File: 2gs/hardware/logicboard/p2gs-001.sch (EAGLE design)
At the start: 66 parts, among them J1 MKR, J10 1-Wire, J2 GPIO, J3 Vcc, J5 SPI, J6 LED, J7 DIN5, K1 G5V1, Q1 220mA/50V/3.5Ω, Q2 220mA/50V/3.5Ω, T1 2SC1815

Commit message: Routed.
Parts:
- removed A, B: (no value), wirepad:SMD2
- removed C1: 22u, rcl:C-EU025-050X050
- removed C10, C11, C4: 100n, rcl:C-EU025-024X044
- removed C12, C13, C3: 1u, rcl:C-EU050-024X044
- removed C2: 470n, rcl:C-EU050-024X044
- removed C5: 10n, resistor:C-EU025-024X044
- removed DISP1: AQM0802A-RN-GBW, AQM0802A-RN-GBW:AQM0802A-RN-GBW
- removed DISP2: MNTR, pinhead:PINHD-1X4
- removed F1: 1.8A, fuse:TE5
- removed H1, H2: STAND-OFF, SparkFun-Hardware:STAND-OFF
- removed J10: 1-Wire, SparkFun-Connectors:CONN_03JST-PTH-VERT
- removed J20: (no value), SparkFun-Connectors:CONN_041.27MM
- removed J3: Vcc, SparkFun-Connectors:CONN_02JST-PTH-2
- removed J5: SPI, SparkFun-Connectors:CONN_061.27MM
- removed J6: LED, SparkFun-Connectors:CONN_03JST-PTH-VERT
- removed JP1: PWRSEL, pinhead:PINHD-2X3
- removed JP2: RTC, SparkFun-Connectors:CONN_05
- removed JP4: RLYJMP, pinhead:PINHD-1X2
- removed JP5: PWR, pinhead:PINHD-1X3
- removed JP6: LED, pinhead:PINHD-1X3
- removed K1: G5V1, relay:G5V1
- removed R1, R3: 1k, resistor:R-EU_0204/5
- removed R101, R102, R103, R104: 10k, rcl:R-EU_M2012
- removed R2: 47k, resistor:R-EU_0204/5
- removed RN2: 4.7k, resistor-net:RN04
- removed RN4: 220, resistor-dil:8R-N
- removed RZ1***, RZ2***, RZ3**, RZ4**, VCCBRIDGE***: Inf, rcl:R-EU_M2012
- removed T1: 2SC1815, transistor:2SC1815
- removed V1: 5V, v-reg:78XXL
- removed VDDBRIDGE: 0, rcl:R-EU_M2012
- added D10, D11, D12, D13, D14, D15, D16, D4, D5, D6, D7, D8, D9: 200mA/100V/1V, SparkFun-DiscreteSemi:DIODE-1N4148
- added D20: DIODE-1N4148, SparkFun-DiscreteSemi:DIODE-1N4148
- added LD1: Red/Green, led:DUOLED-RG-C
- added Q10, Q11, Q12, Q13, Q14, Q15, Q16, Q3, Q4, Q5, Q6, Q7, Q8, Q9: 60V/32A/35mΩ, SparkFun-DiscreteSemi:MOSFET-NCH-FQP30N06L
- added R6: 220, resistor:R-EU_0204/5
- added X1: ADAFRUIT-PCA9685, adafruit-pca9685:ADAFRUIT-PCA9685
- D1, D2, D3: value DIODE-1N4148 -> 200mA/100V/1V
- J0: value (none) -> 12V
- J2: value GPIO -> (none); device SparkFun-Connectors:CONN_04JST-PTH -> Connector:TWIG-4P-2.0'90D'
- Q1, Q2: value 220mA/50V/3.5Ω -> 60V/32A/35mΩ; device SparkFun-DiscreteSemi:MOSFET-NCH-BSS138 -> SparkFun-DiscreteSemi:MOSFET-NCH-FQP30N06L
- R4, R5: value 1k -> 330
- SV2: value (none) -> LD
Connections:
- removed net CAP1N: C12.2, DISP1.3
- removed net CAP1P: C12.1, DISP1.4
- removed net LCDVOUT: C13.2, DISP1.2
- removed net MNTRA: OK1B.A2, RN4A.2
- removed net NMO2RTN: RN2.5
- removed net NMORTN: RN2.4
- removed net NMTRTN: RN2.3
- removed net RLYDRV: R1.1, R2.2, T1.B
- removed net RLYOUT: K12.S
- removed net RLYOUT1: RZ3**.2
- removed net RLYOUT2: RZ4**.2
- removed net RLYSNK: D2.A, K11.2, T1.C
- removed net SCL3V: DISP1.8, Q1.S, R102.1, RZ1***.2
- removed net SDA3V: DISP1.7, Q2.S, R104.1, RZ2***.2
- removed net V+: C1.1, C2.1, D1.C, J0.3, JP1.1, JP5.3, V1.IN
- removed net VCC/2: JP1.5, R3.2, RN4A.1
- removed net VCC/VDD: C11.1, C13.1, DISP1.5, DISP1.9, VCCBRIDGE***.1, VDDBRIDGE.1
- removed net VOUT: F1.2, JP1.4, JP1.6
- removed net VOUTRAW: B.P, C3.1, C4.1, D1.A, J3.2, JP4.2, K12.P, K12.P@1, RZ3**.1, V1.OUT
- removed net VOUTRAW2: A.P, F1.1, JP4.1, K12.O, RZ4**.1
- new net LD00: D1.A, Q1.D, SV2-1.S
- new net LD01: D2.A, Q2.D, SV2-3.S
- new net LD02: D3.A, Q3.D, SV2-5.S
- new net LD03: D4.A, Q4.D, SV2-7.S
- new net LD04: D5.A, Q5.D, SV2-9.S
- new net LD05: D6.A, Q6.D, SV2-11.S
- new net LD06: D7.A, Q7.D, SV2-13.S
- new net LD07: D8.A, Q8.D, SV2-15.S
- new net LD08: D9.A, Q9.D, SV2-17.S
- new net LD09: D10.A, Q10.D, SV2-19.S
- new net LD10: D11.A, Q11.D, SV2-21.S
- new net LD11: D12.A, Q12.D, SV2-23.S
- new net LD12: D13.A, Q13.D, SV2-25.S
- new net LD13: D14.A, Q14.D, SV2-27.S
- new net LD14: D15.A, Q15.D, SV2-29.S
- new net LD15: D16.A, Q16.D, SV2-31.S
- new net PWM00: Q1.G, X1.13
- new net PWM01: Q2.G, X1.14
- new net PWM02: Q3.G, X1.15
- new net PWM03: Q4.G, X1.16
- new net PWM04: Q5.G, X1.17
- new net PWM05: Q6.G, X1.18
- new net PWM06: Q7.G, X1.19
- new net PWM07: Q8.G, X1.20
- new net PWM08: Q9.G, X1.21
- new net PWM09: Q10.G, X1.22
- new net PWM10: Q11.G, X1.23
- new net PWM11: Q12.G, X1.24
- new net PWM12: Q13.G, X1.25
- new net PWM13: Q14.G, X1.26
- new net PWM14: Q15.G, X1.27
- new net PWM15: Q16.G, X1.28
- net AREF: no longer C10.1, R3.1
- net GND: now also J2.4, LD1.C, OK1B.A2, Q1.S, Q10.S, Q11.S, Q12.S, Q13.S, Q14.S, Q15.S, Q16.S, Q2.S, Q3.S, Q4.S, Q5.S, Q6.S, Q7.S, Q8.S, Q9.S, X1.1, X1.2, X1.45, X1.46, X1.47, X1.48, X1.49, X1.50, X1.51, X1.52, X1.53, X1.54, X1.55, X1.56, X1.57, X1.58, X1.59, X1.60, X1.7; no longer C1.2, C10.2, C11.2, C2.2, C3.2, C4.2, C5.2, DISP1.6, DISP2.1, J10.1, J2.1, J3.1, J5.6, J6.2, JP2.2, JP5.1, JP6.2, R2.1, T1.E, V1.GND
- net GPIO0: no longer J2.3, J20.3
- net GPIO1: no longer J2.4, J20.4
- net LED0A: now also LD1.AR; no longer J6.3, JP6.3
- net LED1A: now also LD1.AG; no longer J6.1, JP6.1
- net MIDIINSND: now also D20.C, R6.1; no longer D3.C, RN4B.1
- net MIRTN: now also D20.A; no longer D3.A
- net MISND: now also R6.2; no longer RN4B.2
- net MISO: no longer J5.1
- net MNTR: no longer OK1B.VO2, RN3.5
- net MOSI: no longer J5.4
- net RLY: no longer R1.2
- net RST: no longer J5.5
- net RX: now also RN3.5; no longer RN2.2
- net SCK: no longer J5.3
- net SCL: now also J2.1, X1.3; no longer DISP2.3, JP2.4, Q1.D, R101.1, RZ1***.1
- net SDA: now also J2.2, X1.4; no longer DISP2.4, JP2.5, Q2.D, R103.1, RZ2***.1
- net THS: no longer J10.2, RN3.4
- net VCC: now also J2.3, X1.5; no longer C5.1, D2.C, DISP2.2, J10.3, J2.2, J5.2, JP1.3, JP2.1, JP5.2, K11.1, R101.2, R103.2, RN2.1, VCCBRIDGE***.2
- net VDD: no longer Q1.G, Q2.G, R102.2, R104.2, VDDBRIDGE.2
- net VIN: now also D1.C, D10.C, D11.C, D12.C, D13.C, D14.C, D15.C, D16.C, D2.C, D3.C, D4.C, D5.C, D6.C, D7.C, D8.C, D9.C, J0.3, SV2-10.S, SV2-12.S, SV2-14.S, SV2-16.S, SV2-18.S, SV2-2.S, SV2-20.S, SV2-22.S, SV2-24.S, SV2-26.S, SV2-28.S, SV2-30.S, SV2-32.S, SV2-4.S, SV2-6.S, SV2-8.S, X1.12, X1.29, X1.30, X1.31, X1.32, X1.33, X1.34, X1.35, X1.36, X1.37, X1.38, X1.39, X1.40, X1.41, X1.42, X1.43, X1.44, X1.6; no longer JP1.2
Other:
- moved on the sheet: D1, D2, D3, J0, J1, J7, OK1A, OK1B, Q1, Q2, R4, R5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

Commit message: Artwork.
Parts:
- renumbered D20 to D0, J2 to JG1
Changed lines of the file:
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@@
 <parts>
 <part name="MC1" library="adafruit" deviceset="ARDUINOMICRO" device=""/>
-<part name="D20" library="SparkFun-DiscreteSemi" library_urn="urn:adsk.eagle:library:514" deviceset="DIODE" device="-1N4148" package3d_urn="urn:adsk.eagle:package:38452/1" value=""/>
+<part name="D0" library="SparkFun-DiscreteSemi" library_urn="urn:adsk.eagle:library:514" deviceset="DIODE" device="-1N4148" package3d_urn="urn:adsk.eagle:package:38452/1" value=""/>
 <part name="LOGO1" library="SparkFun-Aesthetics" deviceset="OSHW-LOGO" device="S-COPPER" value="OSHW-LOGOS-COPPER"/>
 <part name="U$1" library="pineapple" deviceset="PINEAPPLE450_SILK" device=""/>
@@
 <part name="SUPPLY28" library="supply2" deviceset="GND" device=""/>
 <part name="SUPPLY30" library="supply2" deviceset="GND" device=""/>
-<part name="J2" library="Connector" deviceset="TWIG-4P-2.0" device="'90D'"/>
+<part name="JG1" library="Connector" deviceset="TWIG-4P-2.0" device="'90D'"/>
 </parts>
 <sheets>
@@
 <instances>
 <instance part="MC1" gate="G$1" x="355.6" y="127" smashed="yes" rot="R270"/>
-<instance part="D20" gate="G$1" x="360.68" y="88.9" smashed="yes" rot="R180">
+<instance part="D0" gate="G$1" x="360.68" y="88.9" smashed="yes" rot="R180">
 <attribute name="NAME" x="360.68" y="83.82" size="1.778" layer="95" align="bottom-center"/>
 <attribute name="VALUE" x="363.22" y="90.932" size="1.778" layer="96" font="vector" rot="R180" align="top-left"/>
@@
 <instance part="SUPPLY28" gate="GND" x="154.94" y="106.68" smashed="yes"/>
 <instance part="SUPPLY30" gate="GND" x="175.26" y="106.68" smashed="yes"/>
-<instance part="J2" gate="G$1" x="299.72" y="71.12" smashed="yes">
+<instance part="JG1" gate="G$1" x="299.72" y="71.12" smashed="yes">
 <attribute name="NAME" x="298.45" y="76.2" size="1.27" layer="95"/>
 <attribute name="VALUE" x="302.26" y="67.31" size="1.27" layer="96" rot="R90"/>
@@
 </segment>
 <segment>
-<pinref part="J2" gate="G$1" pin="4"/>
+<pinref part="JG1" gate="G$1" pin="4"/>
 <wire x1="295.91" y1="67.31" x2="289.56" y2="67.31" width="0.1524" layer="91"/>
 <label x="289.56" y="68.58" size="0.8128" layer="95"/>
@@
 </segment>
 <segment>
-<pinref part="J2" gate="G$1" pin="3"/>
+<pinref part="JG1" gate="G$1" pin="3"/>
 <wire x1="295.91" y1="69.85" x2="289.56" y2="69.85" width="0.1524" layer="91"/>
 <label x="284.48" y="71.12" size="0.8128" layer="95"/>
@@
 <segment>
 <wire x1="353.06" y1="93.98" x2="353.06" y2="91.44" width="0.1524" layer="91"/>
-<pinref part="D20" gate="G$1" pin="C"/>
+<pinref part="D0" gate="G$1" pin="C"/>
 <wire x1="353.06" y1="91.44" x2="353.06" y2="88.9" width="0.1524" layer="91"/>
 <wire x1="353.06" y1="88.9" x2="358.14" y2="88.9" width="0.1524" layer="91"/>
@@
 </segment>
 <segment>
-<pinref part="J2" gate="G$1" pin="2"/>
+<pinref part="JG1" gate="G$1" pin="2"/>
 <wire x1="295.91" y1="72.39" x2="289.56" y2="72.39" width="0.1524" layer="91"/>
 <label x="289.56" y="73.66" size="0.8128" layer="95"/>
@@
 <net name="MIRTN" class="0">
 <segment>
-<pinref part="D20" gate="G$1" pin="A"/>
+<pinref part="D0" gate="G$1" pin="A"/>
 <wire x1="363.22" y1="88.9" x2="365.76" y2="88.9" width="0.1524" layer="91"/>
 <wire x1="365.76" y1="88.9" x2="365.76" y2="86.36" width="0.1524" layer="91"/>
@@
 </segment>
 <segment>
-<pinref part="J2" gate="G$1" pin="1"/>
+<pinref part="JG1" gate="G$1" pin="1"/>
 <wire x1="295.91" y1="74.93" x2="289.56" y2="74.93" width="0.1524" layer="91"/>
 <label x="289.56" y="76.2" size="0.8128" layer="95"/>

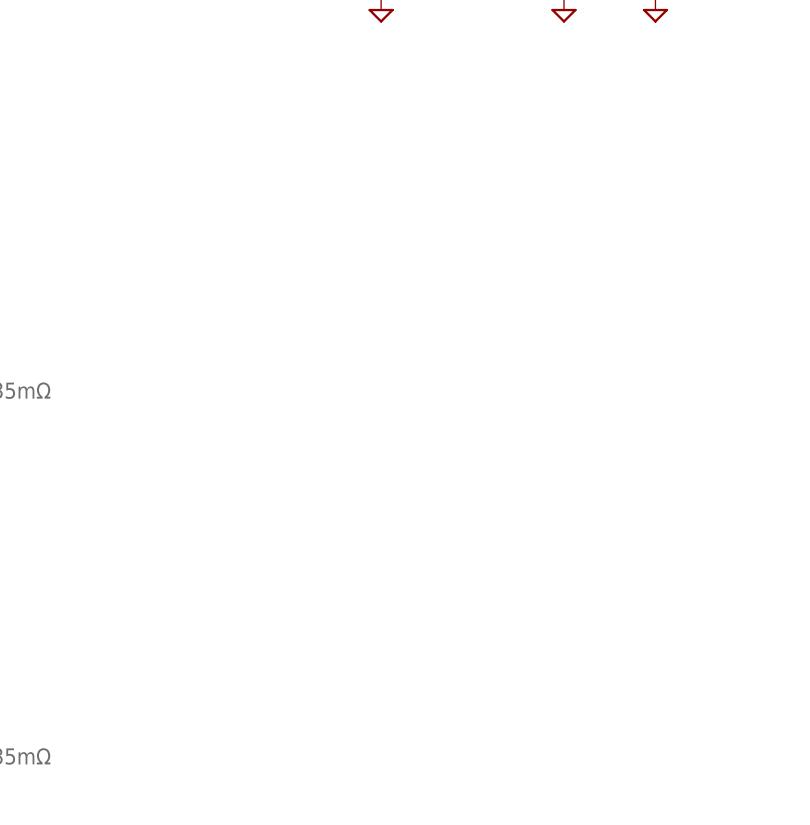
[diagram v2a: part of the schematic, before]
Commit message: Pull-down.
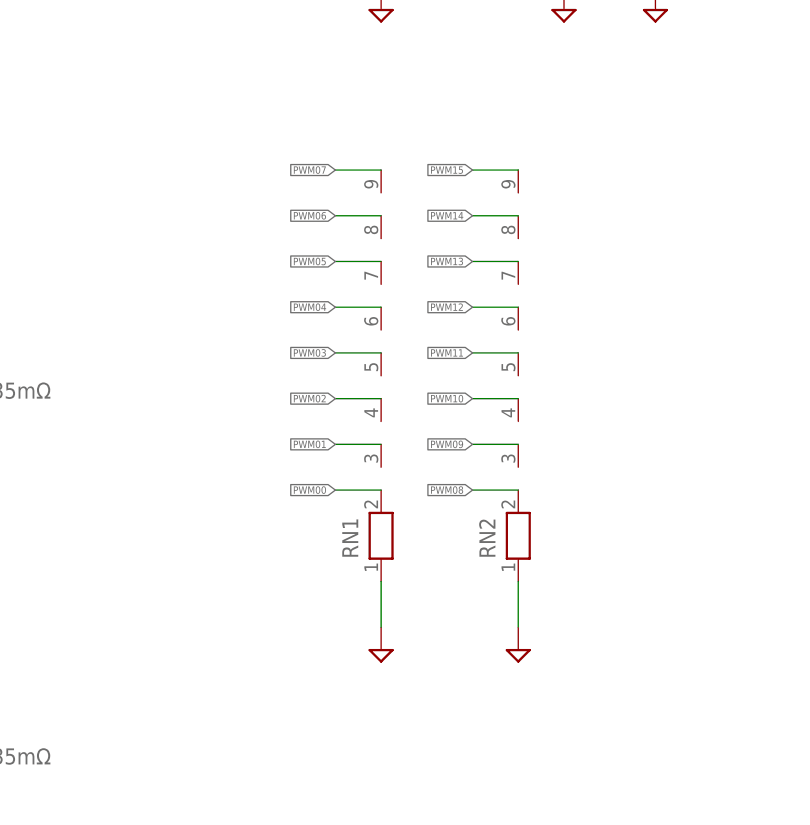
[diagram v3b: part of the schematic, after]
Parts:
- added RN1, RN2: (no value), resistor-net:RN08
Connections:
- net GND: now also RN1.1, RN2.1
- net PWM00: now also RN1.2
- net PWM01: now also RN1.3
- net PWM02: now also RN1.4
- net PWM03: now also RN1.5
- net PWM04: now also RN1.6
- net PWM05: now also RN1.7
- net PWM06: now also RN1.8
- net PWM07: now also RN1.9
- net PWM08: now also RN2.2
- net PWM09: now also RN2.3
- net PWM10: now also RN2.4
- net PWM11: now also RN2.5
- net PWM12: now also RN2.6
- net PWM13: now also RN2.7
- net PWM14: now also RN2.8
- net PWM15: now also RN2.9
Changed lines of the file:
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@@
 <part name="SUPPLY30" library="supply2" deviceset="GND" device=""/>
 <part name="JG1" library="Connector" deviceset="TWIG-4P-2.0" device="'90D'"/>
+<part name="RN1" library="resistor-net" library_urn="urn:adsk.eagle:library:343" deviceset="RN08" device="" package3d_urn="urn:adsk.eagle:package:24977/1"/>
+<part name="RN2" library="resistor-net" library_urn="urn:adsk.eagle:library:343" deviceset="RN08" device="" package3d_urn="urn:adsk.eagle:package:24977/1"/>
+<part name="SUPPLY31" library="supply2" deviceset="GND" device=""/>
+<part name="SUPPLY32" library="supply2" deviceset="GND" device=""/>
 </parts>
 <sheets>
@@
 <attribute name="VALUE" x="302.26" y="67.31" size="1.27" layer="96" rot="R90"/>
 </instance>
+<instance part="RN1" gate="1" x="231.14" y="139.7" smashed="yes" rot="R90">
+<attribute name="NAME" x="228.6" y="137.16" size="1.778" layer="95" rot="R90"/>
+<attribute name="VALUE" x="235.458" y="137.16" size="1.778" layer="96" rot="R90"/>
+</instance>
+<instance part="RN2" gate="1" x="246.38" y="139.7" smashed="yes" rot="R90">
+<attribute name="NAME" x="243.84" y="137.16" size="1.778" layer="95" rot="R90"/>
+<attribute name="VALUE" x="250.698" y="137.16" size="1.778" layer="96" rot="R90"/>
+</instance>
+<instance part="SUPPLY31" gate="GND" x="231.14" y="127" smashed="yes"/>
+<instance part="SUPPLY32" gate="GND" x="246.38" y="127" smashed="yes"/>
 </instances>
 <busses>
@@
 <wire x1="295.91" y1="67.31" x2="289.56" y2="67.31" width="0.1524" layer="91"/>
 <label x="289.56" y="68.58" size="0.8128" layer="95"/>
+</segment>
+<segment>
+<pinref part="RN1" gate="1" pin="1"/>
+<wire x1="231.14" y1="134.62" x2="231.14" y2="129.54" width="0.1524" layer="91"/>
+<pinref part="SUPPLY31" gate="GND" pin="GND"/>
+</segment>
+<segment>
+<pinref part="RN2" gate="1" pin="1"/>
+<wire x1="246.38" y1="134.62" x2="246.38" y2="129.54" width="0.1524" layer="91"/>
+<pinref part="SUPPLY32" gate="GND" pin="GND"/>
 </segment>
 </net>
@@
 <label x="22.86" y="154.94" size="0.8128" layer="95" rot="R180" xref="yes"/>
 </segment>
+<segment>
+<pinref part="RN1" gate="1" pin="2"/>
+<wire x1="231.14" y1="144.78" x2="226.06" y2="144.78" width="0.1524" layer="91"/>
+<label x="226.06" y="144.78" size="0.8128" layer="95" rot="R180" xref="yes"/>
+</segment>
 </net>
 <net name="PWM01" class="0">
@@
 <label x="43.18" y="154.94" size="0.8128" layer="95" rot="R180" xref="yes"/>
 </segment>
+<segment>
+<pinref part="RN1" gate="1" pin="3"/>
+<wire x1="231.14" y1="149.86" x2="226.06" y2="149.86" width="0.1524" layer="91"/>
+<label x="226.06" y="149.86" size="0.8128" layer="95" rot="R180" xref="yes"/>
+</segment>
 </net>
 <net name="PWM02" class="0">
@@
 <label x="63.5" y="154.94" size="0.8128" layer="95" rot="R180" xref="yes"/>
 </segment>
+<segment>
+<pinref part="RN1" gate="1" pin="4"/>
+<wire x1="231.14" y1="154.94" x2="226.06" y2="154.94" width="0.1524" layer="91"/>
+<label x="226.06" y="154.94" size="0.8128" layer="95" rot="R180" xref="yes"/>
+</segment>
 </net>
 <net name="PWM03" class="0">
@@
 <label x="83.82" y="154.94" size="0.8128" layer="95" rot="R180" xref="yes"/>
 </segment>
+<segment>
+<pinref part="RN1" gate="1" pin="5"/>
+<wire x1="231.14" y1="160.02" x2="226.06" y2="160.02" width="0.1524" layer="91"/>
+<label x="226.06" y="160.02" size="0.8128" layer="95" rot="R180" xref="yes"/>
+</segment>
 </net>
 <net name="PWM04" class="0">
@@
 <label x="104.14" y="154.94" size="0.8128" layer="95" rot="R180" xref="yes"/>
 </segment>
+<segment>
+<pinref part="RN1" gate="1" pin="6"/>
+<wire x1="231.14" y1="165.1" x2="226.06" y2="165.1" width="0.1524" layer="91"/>
+<label x="226.06" y="165.1" size="0.8128" layer="95" rot="R180" xref="yes"/>
+</segment>
 </net>
 <net name="PWM05" class="0">
@@
 <label x="124.46" y="154.94" size="0.8128" layer="95" rot="R180" xref="yes"/>
 </segment>
+<segment>
+<pinref part="RN1" gate="1" pin="7"/>
+<wire x1="231.14" y1="170.18" x2="226.06" y2="170.18" width="0.1524" layer="91"/>
+<label x="226.06" y="170.18" size="0.8128" layer="95" rot="R180" xref="yes"/>
+</segment>
 </net>
 <net name="PWM06" class="0">
@@
 <label x="144.78" y="154.94" size="0.8128" layer="95" rot="R180" xref="yes"/>
 </segment>
+<segment>
+<pinref part="RN1" gate="1" pin="8"/>
+<wire x1="231.14" y1="175.26" x2="226.06" y2="175.26" width="0.1524" layer="91"/>
+<label x="226.06" y="175.26" size="0.8128" layer="95" rot="R180" xref="yes"/>
+</segment>
 </net>
 <net name="PWM07" class="0">
@@
 <label x="165.1" y="154.94" size="0.8128" layer="95" rot="R180" xref="yes"/>
 </segment>
+<segment>
+<pinref part="RN1" gate="1" pin="9"/>
+<wire x1="231.14" y1="180.34" x2="226.06" y2="180.34" width="0.1524" layer="91"/>
+<label x="226.06" y="180.34" size="0.8128" layer="95" rot="R180" xref="yes"/>
+</segment>
 </net>
 <net name="PWM08" class="0">
@@
 <label x="22.86" y="114.3" size="0.8128" layer="95" rot="R180" xref="yes"/>
 </segment>
+<segment>
+<pinref part="RN2" gate="1" pin="2"/>
+<wire x1="246.38" y1="144.78" x2="241.3" y2="144.78" width="0.1524" layer="91"/>
+<label x="241.3" y="144.78" size="0.8128" layer="95" rot="R180" xref="yes"/>
+</segment>
 </net>
 <net name="PWM09" class="0">
@@
 <label x="43.18" y="114.3" size="0.8128" layer="95" rot="R180" xref="yes"/>
 </segment>
+<segment>
+<pinref part="RN2" gate="1" pin="3"/>
+<wire x1="246.38" y1="149.86" x2="241.3" y2="149.86" width="0.1524" layer="91"/>
+<label x="241.3" y="149.86" size="0.8128" layer="95" rot="R180" xref="yes"/>
+</segment>
 </net>
 <net name="PWM10" class="0">
@@
 <label x="63.5" y="114.3" size="0.8128" layer="95" rot="R180" xref="yes"/>
 </segment>
+<segment>
+<pinref part="RN2" gate="1" pin="4"/>
+<wire x1="246.38" y1="154.94" x2="241.3" y2="154.94" width="0.1524" layer="91"/>
+<label x="241.3" y="154.94" size="0.8128" layer="95" rot="R180" xref="yes"/>
+</segment>
 </net>
 <net name="PWM11" class="0">
@@
 <label x="83.82" y="114.3" size="0.8128" layer="95" rot="R180" xref="yes"/>
 </segment>
+<segment>
+<pinref part="RN2" gate="1" pin="5"/>
+<wire x1="246.38" y1="160.02" x2="241.3" y2="160.02" width="0.1524" layer="91"/>
+<label x="241.3" y="160.02" size="0.8128" layer="95" rot="R180" xref="yes"/>
+</segment>
 </net>
 <net name="PWM12" class="0">
@@
 <label x="104.14" y="114.3" size="0.8128" layer="95" rot="R180" xref="yes"/>
 </segment>
+<segment>
+<pinref part="RN2" gate="1" pin="6"/>
+<wire x1="246.38" y1="165.1" x2="241.3" y2="165.1" width="0.1524" layer="91"/>
+<label x="241.3" y="165.1" size="0.8128" layer="95" rot="R180" xref="yes"/>
+</segment>
 </net>
 <net name="PWM13" class="0">
@@
 <label x="124.46" y="114.3" size="0.8128" layer="95" rot="R180" xref="yes"/>
 </segment>
+<segment>
+<pinref part="RN2" gate="1" pin="7"/>
+<wire x1="246.38" y1="170.18" x2="241.3" y2="170.18" width="0.1524" layer="91"/>
+<label x="241.3" y="170.18" size="0.8128" layer="95" rot="R180" xref="yes"/>
+</segment>
 </net>
 <net name="PWM14" class="0">
@@
 <label x="144.78" y="114.3" size="0.8128" layer="95" rot="R180" xref="yes"/>
 </segment>
+<segment>
+<pinref part="RN2" gate="1" pin="8"/>
+<wire x1="246.38" y1="175.26" x2="241.3" y2="175.26" width="0.1524" layer="91"/>
+<label x="241.3" y="175.26" size="0.8128" layer="95" rot="R180" xref="yes"/>
+</segment>
 </net>
 <net name="PWM15" class="0">
@@
 <label x="165.1" y="114.3" size="0.8128" layer="95" rot="R180" xref="yes"/>
 </segment>
-</net>
+<segment>
+<pinref part="RN2" gate="1" pin="9"/>
+<wire x1="246.38" y1="180.34" x2="241.3" y2="180.34" width="0.1524" layer="91"/>
+<label x="241.3" y="180.34" size="0.8128" layer="95" rot="R180" xref="yes"/>
+</segment>
+</net>
